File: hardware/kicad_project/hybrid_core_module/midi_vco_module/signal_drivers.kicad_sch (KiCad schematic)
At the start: 41 parts, among them Q4 2N7002, Q5 BSS83P, U11 TL074, U18 LM4040DBZ-2.5, U19 MCP4922-ESL, U2 TL071, U21 TL074

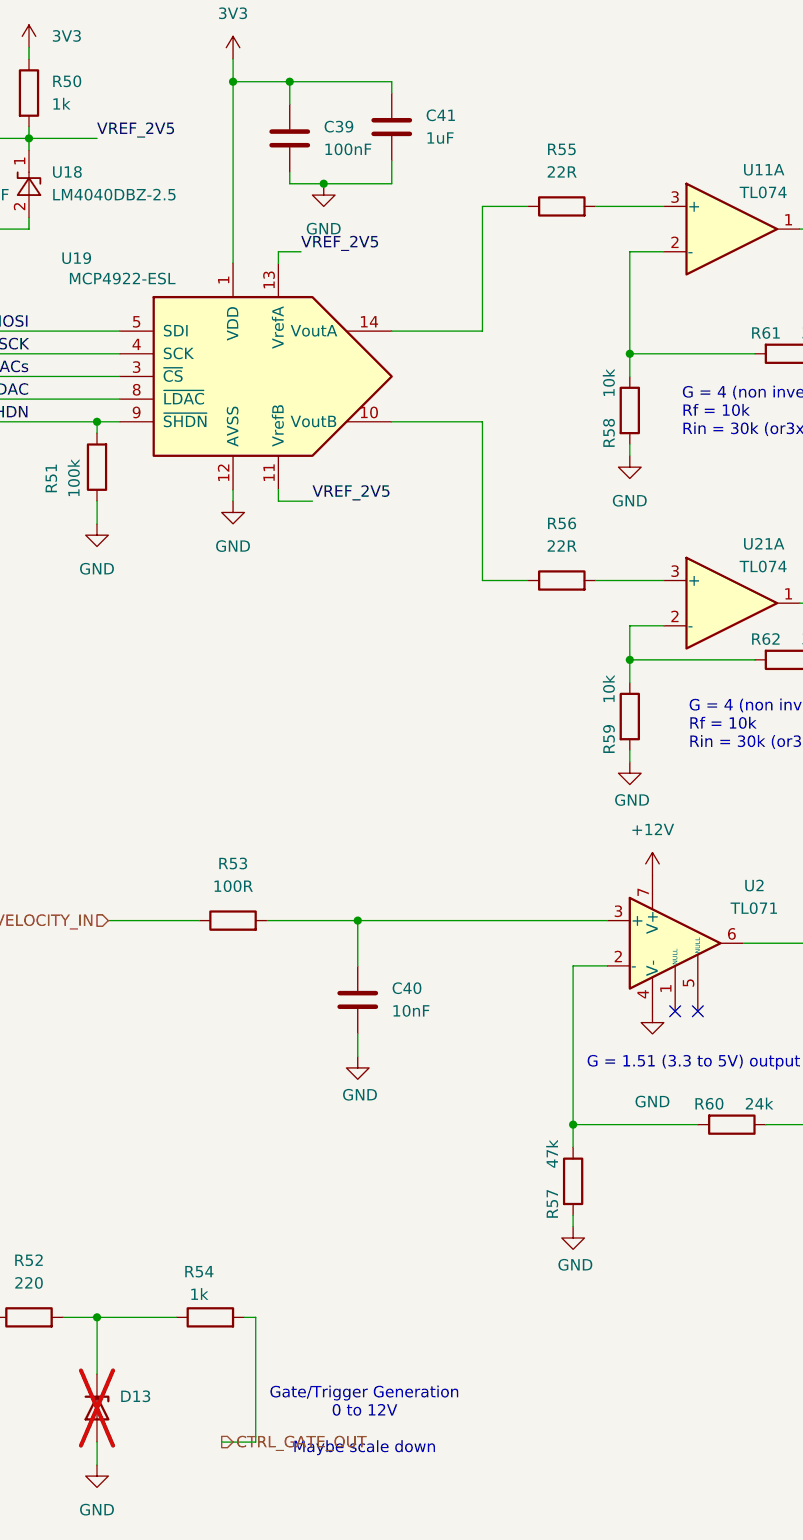
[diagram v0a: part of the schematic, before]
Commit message: Schematic updated. Components Footprint assignment started. Waiting for components mechanical validation before starting layout.
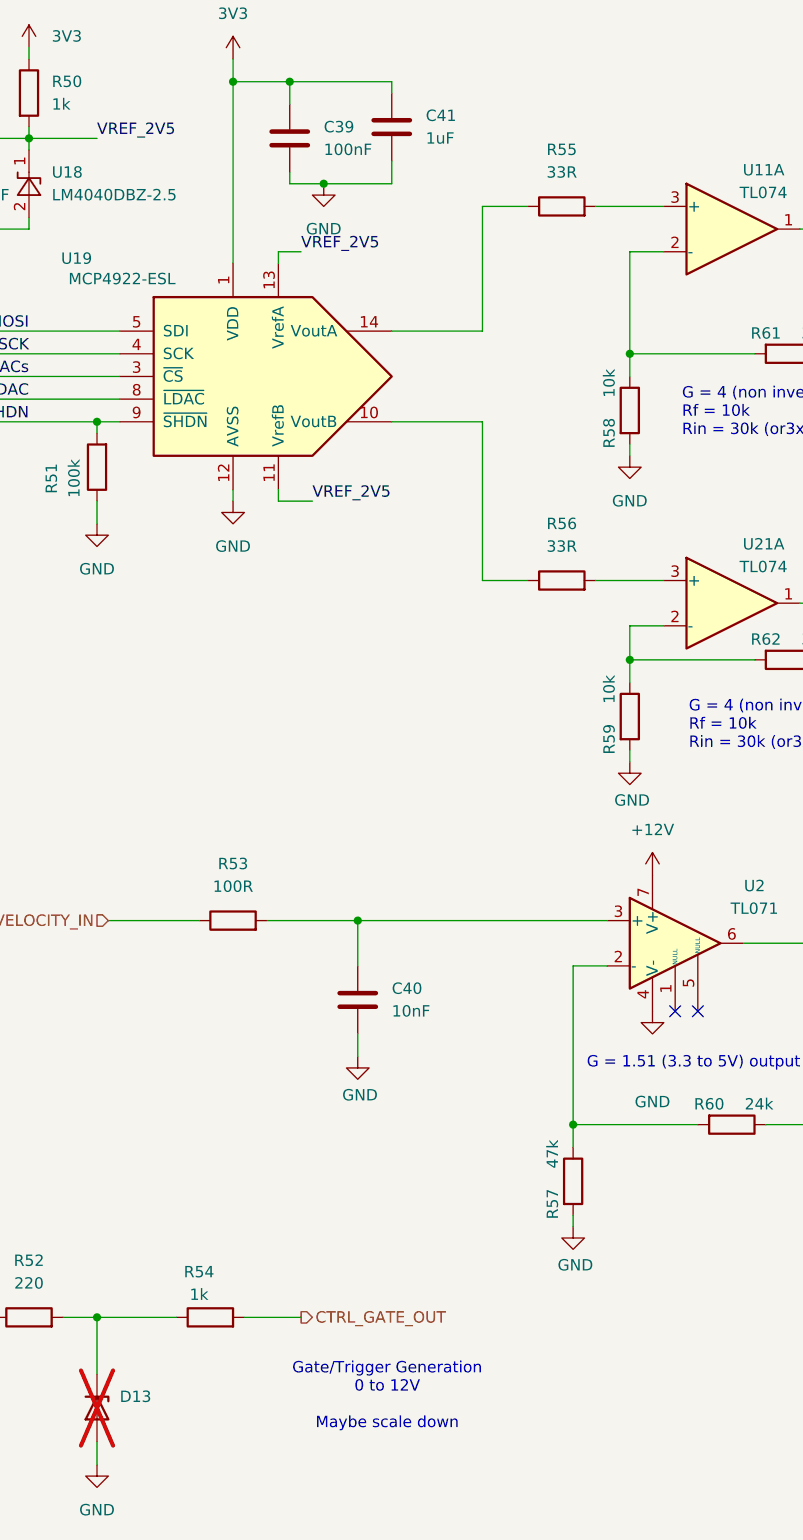
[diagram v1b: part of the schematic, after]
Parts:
- C38, C39, C42, C48, C51, C60, C93: footprint (none) -> Capacitor_SMD:C_0402_1005Metric; Manufacturer (none) -> MURATA; Manufacturer PartNumer (none) -> GRM155R71E104KE14J
- C40: footprint (none) -> Capacitor_SMD:C_0402_1005Metric; Manufacturer (none) -> MURATA; Manufacturer PartNumer (none) -> GRM155R71E103KA01D
- C41, C43, C49, C50, C61, C92: footprint (none) -> Capacitor_SMD:C_0805_2012Metric; Manufacturer (none) -> MURATA; Manufacturer PartNumer (none) -> GRM219R71E105MA88J
- D13: Manufacturer Nexperia -> NEXPERIA
- R47, R48, R51: footprint (none) -> Resistor_SMD:R_0402_1005Metric; Manufacturer (none) -> YAGEO; Manufacturer PartNumer (none) -> RT0402FRE07100KL
- R49, R58, R59: footprint (none) -> Resistor_SMD:R_0402_1005Metric; Manufacturer (none) -> YAGEO; Manufacturer PartNumer (none) -> RT0402FRE0710KL
- R50, R54, R63, R64, R65: footprint (none) -> Resistor_SMD:R_0402_1005Metric; Manufacturer (none) -> YAGEO; Manufacturer PartNumer (none) -> RT0402FRE071KL
- R52: footprint (none) -> Resistor_SMD:R_0402_1005Metric; Manufacturer (none) -> YAGEO; Manufacturer PartNumer (none) -> RT0402FRE07220RL
- R53: footprint (none) -> Resistor_SMD:R_0402_1005Metric; Manufacturer (none) -> YAGEO; Manufacturer PartNumer (none) -> RT0402FRE07100RL
- R55, R56: value 22R -> 33R; footprint (none) -> Resistor_SMD:R_0402_1005Metric; Manufacturer (none) -> YAGEO; Manufacturer PartNumer (none) -> RT0402FRE0733RL
- R57: footprint (none) -> Resistor_SMD:R_0402_1005Metric; Manufacturer (none) -> YAGEO; Manufacturer PartNumer (none) -> RT0402FRE0747KL
- R60: footprint (none) -> Resistor_SMD:R_0402_1005Metric; Manufacturer (none) -> YAGEO; Manufacturer PartNumer (none) -> RT0402FRE0724KL
- R61, R62: footprint (none) -> Resistor_SMD:R_0402_1005Metric; Manufacturer (none) -> YAGEO; Manufacturer PartNumer (none) -> RT0402FRE0730KL

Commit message: - schematic updated  - PN and footprints added
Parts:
- Q4: Manufacturer (none) -> onsemi; Manufacturer PartNumer (none) -> 2N7002
- Q5: Manufacturer (none) -> Infineon Technologies; Manufacturer PartNumer (none) -> BSS83PH6327XTSA1
- U11, U21: footprint (none) -> Package_SO:SOIC-14_3.9x8.7mm_P1.27mm; Manufacturer (none) -> Texas Instruments
- U18: Manufacturer (none) -> Texas Instruments; Manufacturer PartNumer (none) -> LM4040QAIM3-2.5/NOPB
- U19: footprint (none) -> Package_SO:SOIC-14_3.9x8.7mm_P1.27mm; Manufacturer (none) -> Microchip Technology; Manufacturer PartNumer (none) -> MCP4922-E/SL
- U2: Manufacturer (none) -> Texas Instruments; Manufacturer PartNumer (none) -> TL071CDR

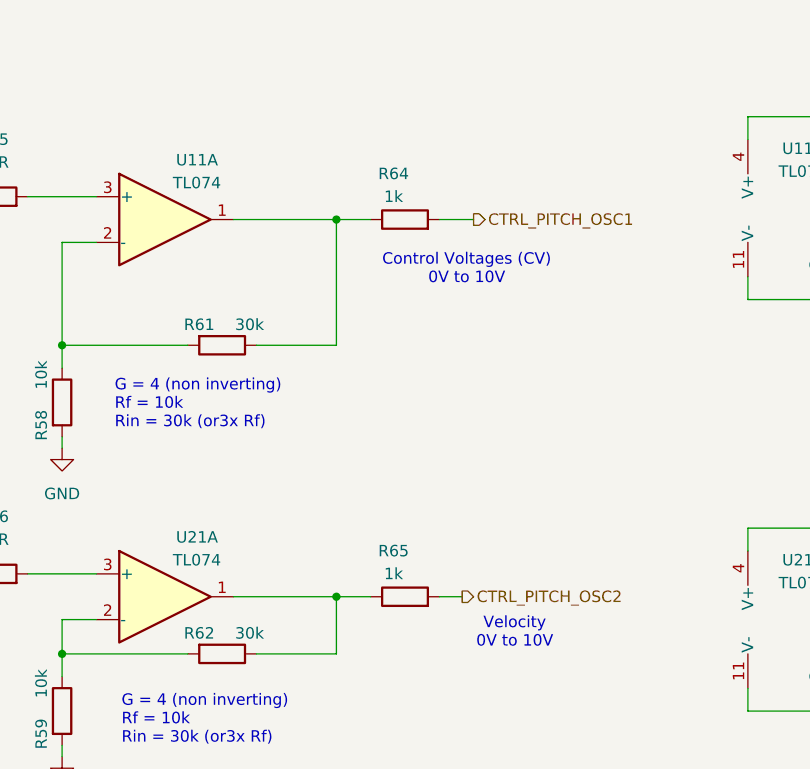
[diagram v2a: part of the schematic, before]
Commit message: components placement (interface) components placement per section
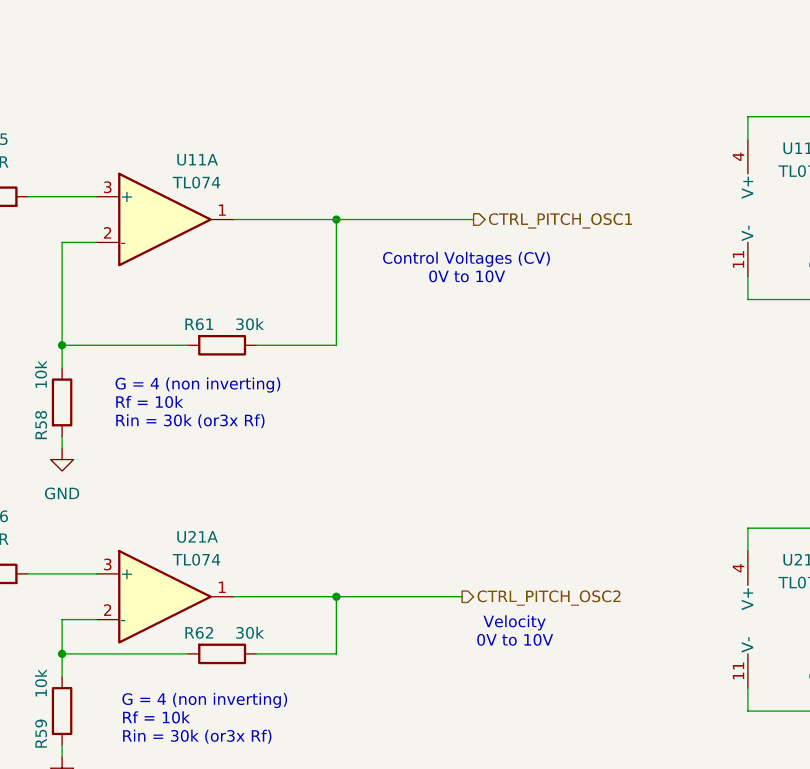
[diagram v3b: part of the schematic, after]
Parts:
- removed R64, R65: 1k, Resistor_SMD:R_0402_1005Metric, symbol Device:R
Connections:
- net CTRL_PITCH_OSC1: now also R61.1, U11.1
- net CTRL_PITCH_OSC2: now also R62.1, U21.1
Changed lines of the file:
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@@
 	(wire
 		(pts
-			(xy 189.23 87.63) (xy 185.42 87.63)
+			(xy 185.42 87.63) (xy 199.39 87.63)
 		)
 		(stroke
@@
 	(wire
 		(pts
-			(xy 196.85 87.63) (xy 199.39 87.63)
-		)
-		(stroke
-			(width 0)
-			(type default)
-		)
-	)
-	(wire
-		(pts
 			(xy 154.94 90.17) (xy 154.94 93.98)
 		)
@@
 	(wire
 		(pts
-			(xy 196.85 45.72) (xy 200.66 45.72)
-		)
-		(stroke
-			(width 0)
-			(type default)
-		)
-	)
-	(wire
-		(pts
 			(xy 176.53 93.98) (xy 185.42 93.98)
 		)
@@
 	(wire
 		(pts
-			(xy 189.23 45.72) (xy 185.42 45.72)
+			(xy 185.42 45.72) (xy 200.66 45.72)
 		)
 		(stroke
@@
 	(symbol
 		(lib_id "Device:R")
-		(at 193.04 45.72 90)
-		(unit 1)
-		(exclude_from_sim no)
-		(in_bom yes)
-		(on_board yes)
-		(dnp no)
-		(property "Reference" "R64"
-			(at 191.77 40.64 90)
-			(effects
-				(font
-					(size 1.27 1.27)
-				)
-			)
-		)
-		(property "Value" "1k"
-			(at 191.77 43.18 90)
-			(effects
-				(font
-					(size 1.27 1.27)
-				)
-			)
-		)
-		(property "Footprint" "Resistor_SMD:R_0402_1005Metric"
-			(at 193.04 47.498 90)
-			(effects
-				(font
-					(size 1.27 1.27)
-				)
-				(hide yes)
-			)
-		)
-		(property "Datasheet" "~"
-			(at 193.04 45.72 0)
-			(effects
-				(font
-					(size 1.27 1.27)
-				)
-				(hide yes)
-			)
-		)
-		(property "Description" "Resistor"
-			(at 193.04 45.72 0)
-			(effects
-				(font
-					(size 1.27 1.27)
-				)
-				(hide yes)
-			)
-		)
-		(property "Manufacturer" "YAGEO"
-			(at 193.04 45.72 90)
-			(effects
-				(font
-					(size 1.27 1.27)
-				)
-				(hide yes)
-			)
-		)
-		(property "Manufacturer PartNumer" "RT0402FRE071KL"
-			(at 193.04 45.72 90)
-			(effects
-				(font
-					(size 1.27 1.27)
-				)
-				(hide yes)
-			)
-		)
-		(property "MN" ""
-			(at 193.04 45.72 90)
-			(effects
-				(font
-					(size 1.27 1.27)
-				)
-				(hide yes)
-			)
-		)
-		(property "MPN" ""
-			(at 193.04 45.72 90)
-			(effects
-				(font
-					(size 1.27 1.27)
-				)
-				(hide yes)
-			)
-		)
-		(pin "2"
-		)
-		(pin "1"
-		)
-		(instances
-			(project "midi_vco_module"
-				(path "/3378c2b5-f4b3-47f0-8cdf-dba4991b82b5/c31db174-6613-4916-a991-4f9ba8b74476"
-					(reference "R64")
-					(unit 1)
-				)
-			)
-			(project "analog_synth"
-				(path "/a8b8d30d-8d60-4de0-b5a6-095005c57c8e/c31db174-6613-4916-a991-4f9ba8b74476"
-					(reference "R39")
-					(unit 1)
-				)
-			)
-		)
-	)
-	(symbol
-		(lib_id "Device:R")
 		(at 154.94 100.33 0)
 		(unit 1)
@@
 					(unit 1)
 				)
-			)
-		)
-	)
-	(symbol
-		(lib_id "Device:R")
-		(at 193.04 87.63 90)
-		(unit 1)
-		(exclude_from_sim no)
-		(in_bom yes)
-		(on_board yes)
-		(dnp no)
-		(property "Reference" "R65"
-			(at 191.77 82.55 90)
-			(effects
-				(font
-					(size 1.27 1.27)
-				)
-			)
-		)
-		(property "Value" "1k"
-			(at 191.77 85.09 90)
-			(effects
-				(font
-					(size 1.27 1.27)
-				)
-			)
-		)
-		(property "Footprint" "Resistor_SMD:R_0402_1005Metric"
-			(at 193.04 89.408 90)
-			(effects
-				(font
-					(size 1.27 1.27)
-				)
-				(hide yes)
-			)
-		)
-		(property "Datasheet" "~"
-			(at 193.04 87.63 0)
-			(effects
-				(font
-					(size 1.27 1.27)
-				)
-				(hide yes)
-			)
-		)
-		(property "Description" "Resistor"
-			(at 193.04 87.63 0)
-			(effects
-				(font
-					(size 1.27 1.27)
-				)
-				(hide yes)
-			)
-		)
-		(property "Manufacturer" "YAGEO"
-			(at 193.04 87.63 90)
-			(effects
-				(font
-					(size 1.27 1.27)
-				)
-				(hide yes)
-			)
-		)
-		(property "Manufacturer PartNumer" "RT0402FRE071KL"
-			(at 193.04 87.63 90)
-			(effects
-				(font
-					(size 1.27 1.27)
-				)
-				(hide yes)
-			)
-		)
-		(property "MN" ""
-			(at 193.04 87.63 90)
-			(effects
-				(font
-					(size 1.27 1.27)
-				)
-				(hide yes)
-			)
-		)
-		(property "MPN" ""
-			(at 193.04 87.63 90)
-			(effects
-				(font
-					(size 1.27 1.27)
-				)
-				(hide yes)
-			)
-		)
-		(pin "2"
-		)
-		(pin "1"
-		)
-		(instances
-			(project "midi_vco_module"
-				(path "/3378c2b5-f4b3-47f0-8cdf-dba4991b82b5/c31db174-6613-4916-a991-4f9ba8b74476"
-					(reference "R65")
-					(unit 1)
-				)
-			)
-			(project "analog_synth"
-				(path "/a8b8d30d-8d60-4de0-b5a6-095005c57c8e/c31db174-6613-4916-a991-4f9ba8b74476"
-					(reference "R40")
-					(unit 1)
-				)
